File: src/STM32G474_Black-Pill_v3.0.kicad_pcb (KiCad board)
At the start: 4 copper layers, 53.3 x 20.3 mm, 48 parts, among them J101 USB_C_Receptacle_USB2.0, J102 Conn_01x20, J103 Conn_01x20, J104 Conn_01x04, SW101 SW_Push, SW102 SW_Push, SW103 SW_Push, U101 W25Q32JVSS, U102 STM32G474CEUx, U103 AP7343xx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

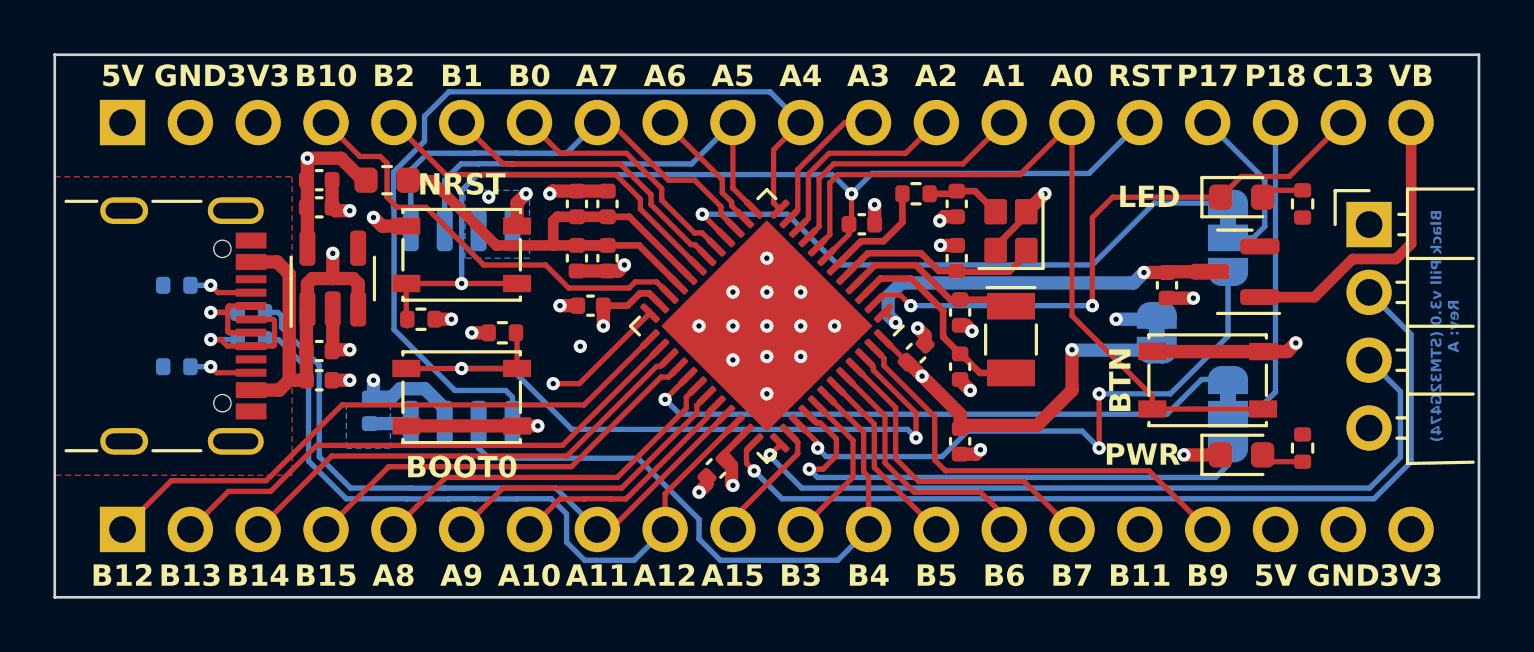
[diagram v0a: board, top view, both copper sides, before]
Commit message: Mod: Moved U102 on the PCB to the programming headers. Re-exported all the files.
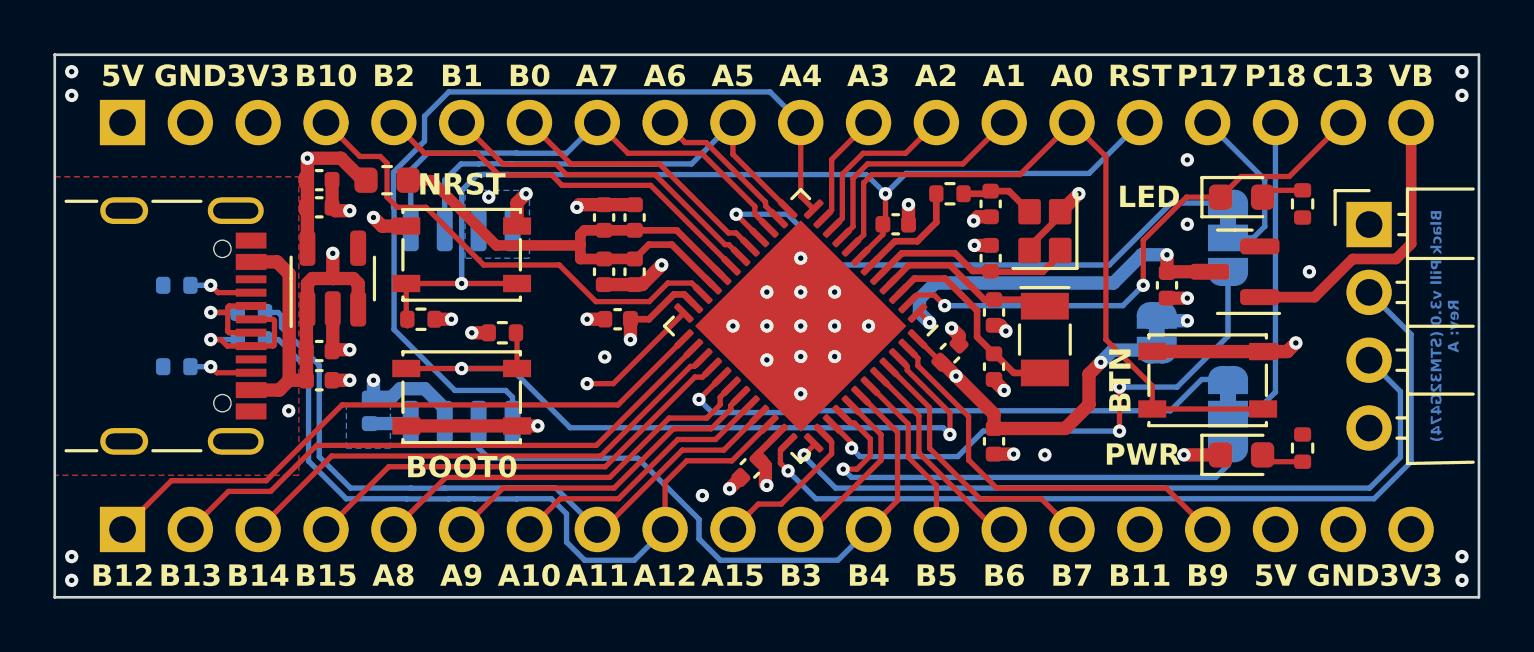
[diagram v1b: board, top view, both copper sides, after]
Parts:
- moved C104 1.27 mm to (130.6, 97.8)
- moved C105 1.27 mm to (134.2, 103.1)
- moved C106 1.27 mm to (134.2, 101.1)
- moved C107 1.27 mm to (134.2, 105.9)
- moved Y101 1.27 mm to (136.1, 98.0)
- moved Y102 1.27 mm to (136.1, 102.1)
- moved C108 1.27 mm to (125.1, 106.9)
- moved U102 1.27 mm to (127.0, 101.6)
- moved C102 1.27 mm to (134.1, 99.1)
- moved C103 1.27 mm to (134.1, 97.0)
- moved C109 1.27 mm to (132.6, 102.6)
- moved R106 1.27 mm to (132.6, 96.6)
- moved C117 1.14 mm to (119.6, 99.6)
- moved C118 1.14 mm to (119.6, 97.5)
- moved C119 1.14 mm to (120.8, 99.6)
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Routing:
- net /PC13: track 22.6 -> 20.4 mm
- net /PC10: track 22.7 -> 20.6 mm
- net /+3.3V_{MCU}: track 37.9 -> 35.9 mm
- net /PA7: track 17.1 -> 18.8 mm
- net /PB11: track 33.1 -> 31.4 mm
- net /PB10: track 17.2 -> 18.9 mm
- net VREF: track 18.7 -> 20.2 mm
- net /PA12: track 26.6 -> 28.1 mm
- net /PB7: track 11.7 -> 10.3 mm
- net /PA15: track 4.74 -> 6.17 mm
- net /PC6: track 23.1 -> 21.7 mm
- net /PB6: track 9.63 -> 8.35 mm
- net /PC11: track 19.9 -> 18.6 mm
- net /PB9: track 16.4 -> 15.1 mm
- net /PA0: track 28.7 -> 27.4 mm
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
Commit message: Fix: Issue with to small annular ring.
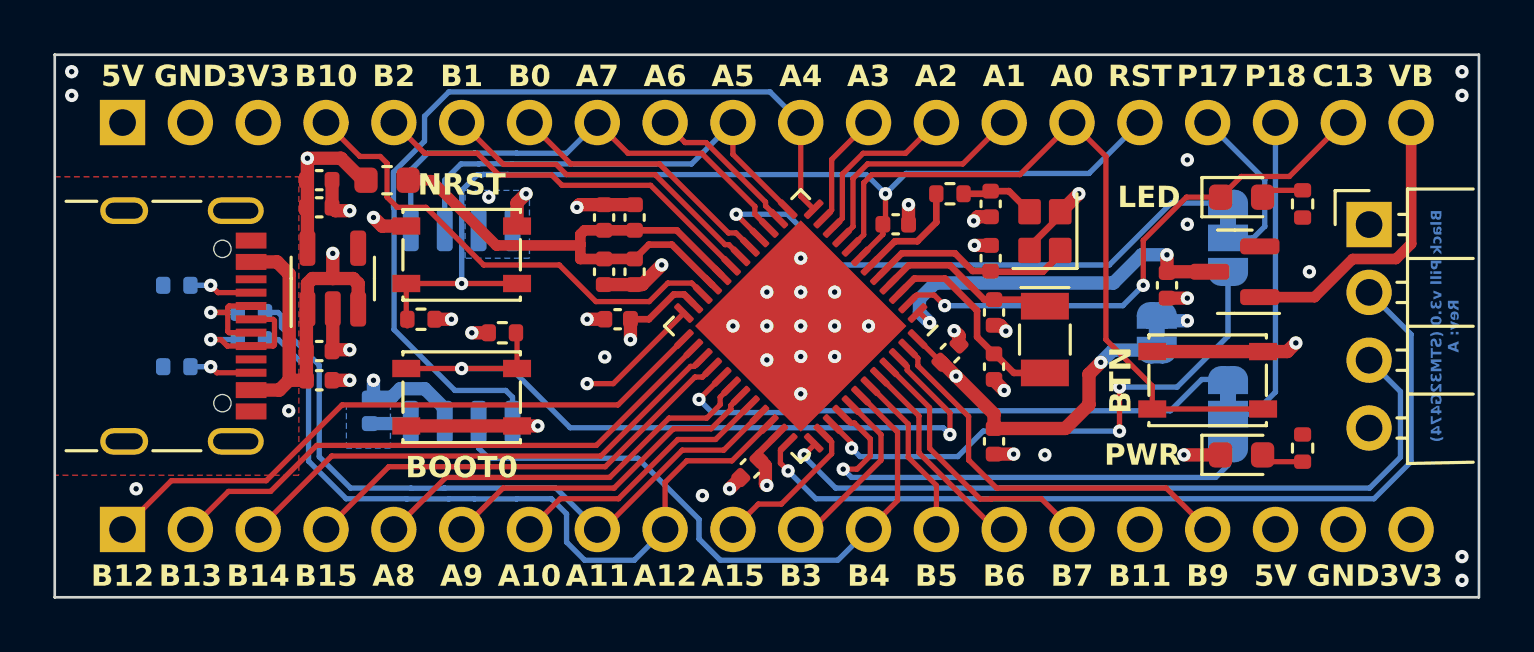
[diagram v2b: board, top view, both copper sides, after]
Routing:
- net +5V: vias 2 -> 1
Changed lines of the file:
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@@
   (via (at 136.144 106.426) (size 0.5) (drill 0.2) (layers "F.Cu" "B.Cu") (net 1))
   (via (at 141.478 97.79) (size 0.5) (drill 0.2) (layers "F.Cu" "B.Cu") (net 1))
-  (via (at 99.695 111.125) (size 0.5) (drill 0.2) (layers "F.Cu" "B.Cu") (net 1))
+  (via (at 102.108 107.696) (size 0.5) (drill 0.2) (layers "F.Cu" "B.Cu") (net 1))
   (via (at 151.765 111.125) (size 0.5) (drill 0.2) (layers "F.Cu" "B.Cu") (net 1))
   (segment (start 140.537 101.406) (end 140.335 101.204) (width 0.5) (layer "B.Cu") (net 1))
@@
   (segment (start 145.22 102.557) (end 144.315 102.557) (width 0.5) (layer "F.Cu") (net 2))
   (segment (start 133.632 97.508) (end 134.112 97.508) (width 0.5) (layer "F.Cu") (net 2))
-  (segment (start 132.927411 101.956305) (end 132.927411 102.276589) (width 0.5) (layer "F.Cu") (net 2))
   (segment (start 110.109 103.632) (end 109.446 103.632) (width 0.5) (layer "F.Cu") (net 2))
   (segment (start 109.446 96.139) (end 109.446 97.155) (width 0.5) (layer "F.Cu") (net 2))
@@
   (segment (start 136.742 97.319) (end 136.719 97.319) (width 0.5) (layer "F.Cu") (net 2))
   (segment (start 109.474 102.51) (end 109.446 102.538) (width 0.5) (layer "F.Cu") (net 2))
+  (segment (start 132.927411 101.956306) (end 132.927411 102.276589) (width 0.5) (layer "F.Cu") (net 2))
   (segment (start 135.569 98.769) (end 135.569 98.619) (width 0.25) (layer "F.Cu") (net 2))
   (segment (start 136.719 97.469) (end 136.719 97.319) (width 0.25) (layer "F.Cu") (net 2))
@@
   (segment (start 145.542 102.235) (end 145.22 102.557) (width 0.5) (layer "F.Cu") (net 2))
   (segment (start 120.777 100.048) (end 121.059 100.048) (width 0.5) (layer "F.Cu") (net 2))
-  (segment (start 132.650139 101.679033) (end 132.927411 101.956305) (width 0.5) (layer "F.Cu") (net 2))
+  (segment (start 132.746069 101.774964) (end 132.927411 101.956306) (width 0.5) (layer "F.Cu") (net 2))
   (segment (start 109.573 97.282) (end 109.446 97.155) (width 0.5) (layer "F.Cu") (net 2))
   (segment (start 118.999 101.346) (end 119.634 101.346) (width 0.5) (layer "F.Cu") (net 2))
@@
   (via (at 133.505 98.58) (size 0.5) (drill 0.2) (layers "F.Cu" "B.Cu") (net 2))
   (via (at 125.73 101.6) (size 0.5) (drill 0.2) (layers "F.Cu" "B.Cu") (net 2))
-  (via (at 132.650139 101.679033) (size 0.5) (drill 0.2) (layers "F.Cu" "B.Cu") (net 2))
+  (via (at 132.746069 101.774964) (size 0.5) (drill 0.2) (layers "F.Cu" "B.Cu") (net 2))
   (via (at 110.109 103.632) (size 0.5) (drill 0.2) (layers "F.Cu" "B.Cu") (net 2))
   (via (at 128.27 101.6) (size 0.5) (drill 0.2) (layers "F.Cu" "B.Cu") (net 2))
@@
   (segment (start 110.424 100.01) (end 110.236 99.822) (width 0.5) (layer "F.Cu") (net 9))
   (segment (start 108.486 103.632) (end 108.486 100.9975) (width 0.5) (layer "F.Cu") (net 9))
-  (via (at 99.695 110.236) (size 0.5) (drill 0.2) (layers "F.Cu" "B.Cu") (net 9))
   (via (at 109.474 98.879076) (size 0.5) (drill 0.2) (layers "F.Cu" "B.Cu") (net 9))
   (segment (start 99.695 95.885) (end 99.695 109.855) (width 0.5) (layer "In2.Cu") (net 9))

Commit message: Mod: Schematic_A.pdf, renamed VREF to VDDA
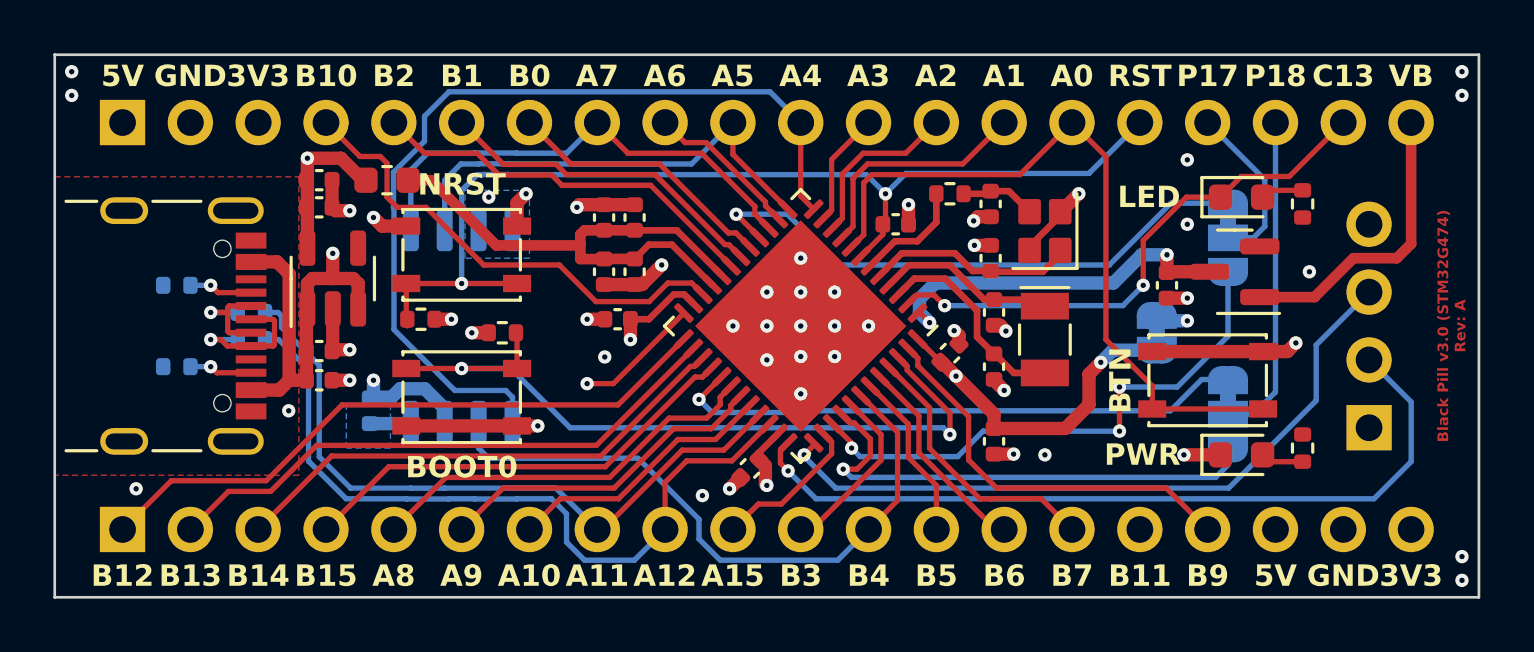
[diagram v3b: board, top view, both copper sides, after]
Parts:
- J104: moved to B.Cu
- moved J104 7.61 mm to (148.3, 105.4)
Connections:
- net VREF renamed VDDA
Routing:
- net /SWDIO: track 32.6 -> 30.1 mm
- net /SWCLK: track 28.1 -> 26.6 mm
